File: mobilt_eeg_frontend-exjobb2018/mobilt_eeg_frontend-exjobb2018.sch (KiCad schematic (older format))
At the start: 86 parts, among them J1 Conn_02x04_Odd_Even, J2 Conn_02x08_Odd_Even, J3 Conn_02x08_Odd_Even, P1 Conn_02x20_Odd_Even, U1 ADS1299-4PAG, X1 X1G0044810050_SG7050CAN_2.048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

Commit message: Before annotation.
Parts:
- added J?: Conn_01x01, symbol Connector_Generic:Conn_01x01
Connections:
- wire segments 307 -> 308
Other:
- note added: "Test Point INTERNAL_VREF 4.5V"
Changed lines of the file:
@@
 Text Label 3950 5550 2    50   ~ 0
 IN8P
+$Comp
+L Connector_Generic:Conn_01x01 J?
+U 1 1 5BD5918B
+P 14000 6100
+F 0 "J?" H 14080 6142 50  0000 L CNN
+F 1 "Conn_01x01" H 14080 6051 50  0000 L CNN
+F 2 "" H 14000 6100 50  0001 C CNN
+F 3 "~" H 14000 6100 50  0001 C CNN
+	1    14000 6100
+	1    0    0    -1
+$EndComp
+Text Notes 14200 6100 0    50   ~ 0
+Test Point INTERNAL_VREF 4.5V
+Wire Wire Line
+	13800 6100 13500 6100
+Connection ~ 13500 6100
 $EndSCHEMATC

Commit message: beginning to understand the big picture... life, the universe, everything...
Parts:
- added C? (x9): 4.7nF, symbol Device:C_Small
- added J?: Conn_02x04_Odd_Even, symbol Connector_Generic:Conn_02x04_Odd_Even
- added J?: INT_CLK, symbol Connector_Generic:Conn_01x02
- added J?: Conn_01x10, symbol Connector_Generic:Conn_01x10
- added R? (x5): 10k, symbol Device:R
- added R? (x10): 4.99k 1%, symbol Device:R_Small
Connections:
- net labels added: CLKSEL
- wire segments 308 -> 360
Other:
- note added: "100nF not in datasheet."
- note added: ">=10k pulldown"
- note added: "Bias Signals"
- note added: "Electrodes [HIGH]/BIAS Header + filtering"
- note added: "Electrodes [LOW]/SRB Header + filtering"
- note added: "Feedback Elements\n(ch.9.3.2.4.1) \nTyp. values for example only"
- note added: "Pull down; DEFAULT EXT. CLK"
- note removed: "Bias Signals\nCHECK THIS SHIT"
- note removed: "Electrode Headers"
- moved on the sheet: C?, J?, R?, U?

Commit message: back it up my dude
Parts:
- removed J2, J3: Conn_02x08_Odd_Even, Pin_Headers:Pin_Header_Straight_2x08_Pitch2.54mm, symbol Connector_Generic:Conn_02x08_Odd_Even
- removed J?: Conn_02x20_Odd_Even, symbol Connector_Generic:Conn_02x20_Odd_Even
- removed J? (x2): Conn_01x10, symbol Connector_Generic:Conn_01x10
- removed R?: 4.99k 1%, symbol Device:R_Small
- added Cf: 1.5nF, symbol Device:C
- added J?: Conn_01x02, symbol Connector_Generic:Conn_01x02
- added J?: Data Header, symbol Connector_Generic:Conn_01x10
- added J? (x2): Conn_01x01, symbol Connector_Generic:Conn_01x01
- added J?: Conn_02x20_Odd_Even, symbol Connector_Generic:Conn_02x20_Odd_Even
- added Rf: 1M, symbol Device:R
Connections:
- net labels added: +3V3_Pi, BIASOUT_FILTERED, SRB1_FILT, SRB2_FILT
- wire segments 360 -> 387
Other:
- note added: "<-In case we need to bypass external reg."
- note added: "Bias Amp\nDC gain\n-(Rf*N)/330k)\n,where N channels."
- note added: "Bias/reference Signals"
- note added: "Cf sets bandwidth\nof Bias Amp."
- note added: "Data Header"
- note added: "Do Not Populate \nfor ADS1299-4!"
- note added: "Electrodes [HIGH]/BIASOUT Header + filtering"
- note added: "External BIASREF circuitry?"
- note added: "For 4ch., Rf=500k?"
- note added: "In case we need to bypass extern reg."
- note added: "Necessary??"
- note added: "PULLUP??"
- note added: "Post-Input filtering \n(ease of measurement)"
- note added: "Test Pad INTERNAL_VREF 4.5V"
- note added: "VCAP1 & 4 closest to ADS1299"
- note added: "VCAP1 Tantalum (not piezoelectric)"
- note added: "Yes, indeed..."
- note removed: "100nF not in datasheet."
- note removed: "ADC Bypassing/Filtering"
- note removed: "Bias Signals"
- note removed: "Electrodes [HIGH]/BIAS Header + filtering"
- note removed: "Tantalum?"
- note removed: "Test Point INTERNAL_VREF 4.5V"
- moved on the sheet: C?, D?, J?, R?, SW?, U?

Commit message: before new annotation
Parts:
- removed C?: 1.5nF, symbol Device:C
- removed J?: Conn_01x02, symbol Connector_Generic:Conn_01x02
- removed R?: 1M, symbol Device:R
- added C? (x5): 1uF, symbol Device:C
- added C? (x3): 100nF, symbol Device:C
- added D?: LED, symbol Device:LED
- added R?: 1k, symbol Device:R
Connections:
- net labels added: AVSS1
- net labels removed: GNDA, VSSA
- wire segments 387 -> 500
- no-connect marks 26 -> 24
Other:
- note added: "<-Regular"
- note added: "BIASIN left floating."
- note added: "From Pin descriptions\nch.6"
- note added: "RasPi Status LED 1"
- note added: "RasPi Status LED 2"
- note added: "Use 3mm THD\nuntil SMD package size\nresolved."
- note added: "pin 53"
- note added: "pin 54"
- note added: "pin 58"
- note added: "pin 59"
- note removed: "External BIASREF circuitry?"
- note removed: "Necessary??"
- note removed: "RasPi Status LED"
- moved on the sheet: C?, J?, R?, U?

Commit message: assigned PCB footprints
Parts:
- C10, C11, C12, C13, C14, C15, C16, C17, C18, C19, C2, C20, C21, C22, C23, C24, C25, C26, C27, C28, C29, C3, C30, C31, C32, C33, C34, C35, C36, C37, C38, C39, C4, C40, C41, C42, C43, C44, C48, C49, C5, C50, C51, C52, C53, C54, C55, C56, C57, C58, C59, C6, C60, C61, C7, C8, C9: renamed from C?; footprint (none) -> Capacitors_SMD:C_0805_HandSoldering
- C46, C47: renamed from C?; footprint (none) -> Capacitors_Tantalum_SMD:CP_Tantalum_Case-D_EIA-7343-31_Hand
- Cf1: renamed from Cf; footprint (none) -> Capacitors_SMD:C_0805_HandSoldering
- D1, D2: renamed from D?; footprint (none) -> LEDs:LED_D3.0mm
- J10, J6: renamed from J?; footprint (none) -> TestPoint:TestPoint_Pad_D2.0mm
- J11, J7: renamed from J?; footprint (none) -> Pin_Headers:Pin_Header_Straight_1x02_Pitch2.54mm
- J12, J4: renamed from J?; footprint (none) -> Pin_Headers:Pin_Header_Straight_1x01_Pitch2.54mm
- J2: renamed from J?; footprint (none) -> Pin_Headers:Pin_Header_Straight_2x20_Pitch2.54mm
- J3: renamed from J?; footprint (none) -> Pin_Headers:Pin_Header_Straight_2x04_Pitch2.54mm
- J5: renamed from J?; footprint (none) -> Pin_Headers:Pin_Header_Straight_1x10_Pitch2.54mm
- J8: renamed from J?; footprint (none) -> Pin_Headers:Pin_Header_Straight_1x08_Pitch2.54mm
- J9: renamed from J?; footprint (none) -> Pin_Headers:Pin_Header_Straight_1x04_Pitch2.54mm
- R10, R11, R12, R13, R14, R15, R16, R17, R18, R19, R20, R21, R22, R23, R24, R25, R26, R27, R28, R29, R3, R30, R31, R4, R5, R6, R7, R8, R9: renamed from R?; footprint (none) -> Resistors_SMD:R_0805_HandSoldering
- Rf1: renamed from Rf; footprint (none) -> Resistors_SMD:R_0805_HandSoldering
- SW1, SW2: renamed from SW?; footprint (none) -> Buttons_Switches_THT:SW_PUSH_6mm_h5mm
- U6: renamed from U?; footprint (none) -> Housings_SOIC:SOIC-8_3.9x4.9mm_Pitch1.27mm
- gave numbers to parts that had none: 5
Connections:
- wire segments 500 -> 499
- no-connect marks 24 -> 18
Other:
- note added: "DVDD: +3V3\nAVDD: +2V5\nAVSS: -2V5"
- note added: "Data Header \nBetween ADS1299 & RasPi"
- note added: "Probably go with 0805 [2012 metric]"
- note removed: "Data Header"
- moved on the sheet: C10, C11, C12, C2, C3, C32, C33, C34, C35, C36, C37, C38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

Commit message: 1/3 way there...
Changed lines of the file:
@@
 	1    0    0    -1
 $EndComp
-$Comp
-L power:GNDD #PWR0108
-U 1 1 5B46722C
-P 19150 3350
-F 0 "#PWR0108" H 19150 3100 50  0001 C CNN
-F 1 "GNDD" H 19154 3195 50  0000 C CNN
-F 2 "" H 19150 3350 50  0001 C CNN
-F 3 "" H 19150 3350 50  0001 C CNN
-	1    19150 3350
-	1    0    0    -1
-$EndComp
-$Comp
-L power:GNDD #PWR0109
-U 1 1 5B467375
-P 18450 3350
-F 0 "#PWR0109" H 18450 3100 50  0001 C CNN
-F 1 "GNDD" H 18454 3195 50  0000 C CNN
-F 2 "" H 18450 3350 50  0001 C CNN
-F 3 "" H 18450 3350 50  0001 C CNN
-	1    18450 3350
-	1    0    0    -1
-$EndComp
 NoConn ~ 10450 4400
 Text Notes 15000 900  0    50   ~ 0
@@
 	1    0    0    -1
 $EndComp
-Text Label 16000 6400 3    50   ~ 0
-+3V3
 $Comp
 L project_symbols:DGND #PWR0133
@@
 Text Notes 20050 6900 0    50   ~ 0
 Probably go with 0805 [2012 metric]
+$Comp
+L project_symbols:DVDD #PWR0105
+U 1 1 5FFDB454
+P 16000 6400
+F 0 "#PWR0105" H 16000 6250 50  0001 C CNN
+F 1 "DVDD" H 16018 6573 50  0000 C CNN
+F 2 "" H 16000 6400 50  0001 C CNN
+F 3 "" H 16000 6400 50  0001 C CNN
+	1    16000 6400
+	-1   0    0    1
+$EndComp
+$Comp
+L project_symbols:DGND #PWR?
+U 1 1 5FFE450C
+P 19150 3350
+F 0 "#PWR?" H 19150 3100 50  0001 C CNN
+F 1 "DGND" H 19154 3195 50  0000 C CNN
+F 2 "" H 19150 3350 50  0001 C CNN
+F 3 "" H 19150 3350 50  0001 C CNN
+	1    19150 3350
+	1    0    0    -1
+$EndComp
+$Comp
+L project_symbols:DGND #PWR?
+U 1 1 5FFE4612
+P 18450 3350
+F 0 "#PWR?" H 18450 3100 50  0001 C CNN
+F 1 "DGND" H 18454 3195 50  0000 C CNN
+F 2 "" H 18450 3350 50  0001 C CNN
+F 3 "" H 18450 3350 50  0001 C CNN
+	1    18450 3350
+	1    0    0    -1
+$EndComp
 $EndSCHEMATC

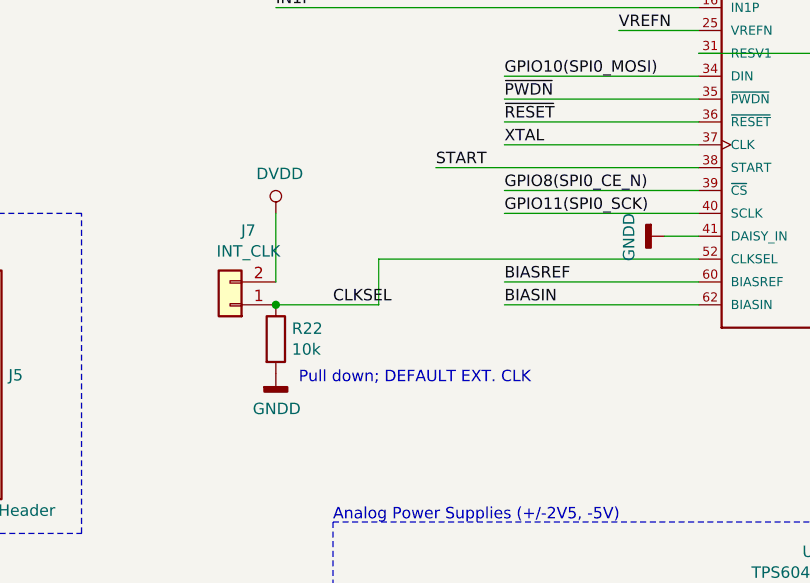
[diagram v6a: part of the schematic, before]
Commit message: took out CLKSEL jumper
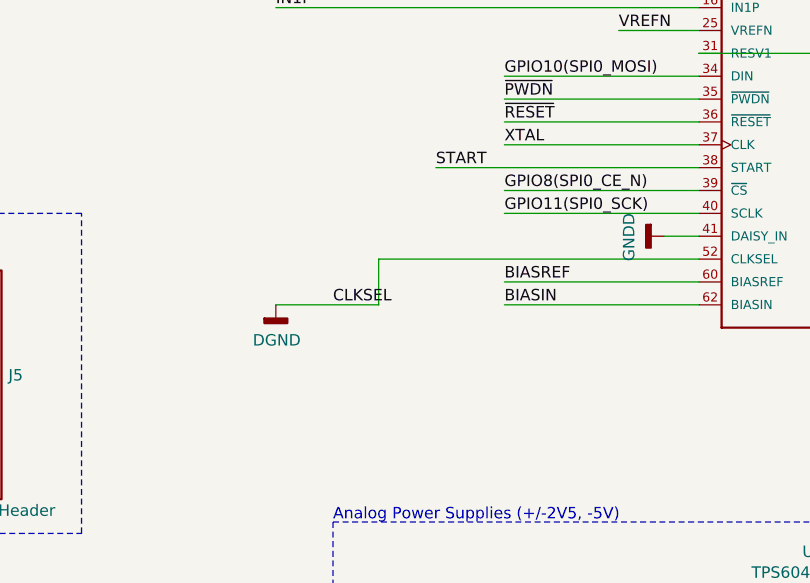
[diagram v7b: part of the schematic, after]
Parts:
- removed J7: INT_CLK, Pin_Headers:Pin_Header_Straight_1x02_Pitch2.54mm, symbol Connector_Generic:Conn_01x02
- removed R22: 10k, Resistors_SMD:R_0805_HandSoldering, symbol Device:R
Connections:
- wire segments 499 -> 498
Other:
- note removed: "Pull down; DEFAULT EXT. CLK"
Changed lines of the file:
@@
 CLKSEL
-$Comp
-L power:GNDD #PWR015
-U 1 1 5B6FFE3E
-P 6800 5500
-F 0 "#PWR015" H 6800 5250 50  0001 C CNN
-F 1 "GNDD" H 6804 5345 50  0000 C CNN
-F 2 "" H 6800 5500 50  0001 C CNN
-F 3 "" H 6800 5500 50  0001 C CNN
-	1    6800 5500
-	1    0    0    -1
-$EndComp
-$Comp
-L Device:R R22
-U 1 1 5B700D8A
-P 6800 5350
-F 0 "R22" H 6870 5396 50  0000 L CNN
-F 1 "10k" H 6870 5305 50  0000 L CNN
-F 2 "Resistors_SMD:R_0805_HandSoldering" V 6730 5350 50  0001 C CNN
-F 3 "~" H 6800 5350 50  0001 C CNN
-	1    6800 5350
-	1    0    0    -1
-$EndComp
-Text Notes 6900 5550 0    50   ~ 0
-Pull down; DEFAULT EXT. CLK
-$Comp
-L Connector_Generic:Conn_01x02 J7
-U 1 1 5B72A277
-P 6600 5200
-F 0 "J7" H 6520 4875 50  0000 C CNN
-F 1 "INT_CLK" H 6520 4966 50  0000 C CNN
-F 2 "Pin_Headers:Pin_Header_Straight_1x02_Pitch2.54mm" H 6600 5200 50  0001 C CNN
-F 3 "~" H 6600 5200 50  0001 C CNN
-	1    6600 5200
-	-1   0    0    1
-$EndComp
-Connection ~ 6800 5200
-$Comp
-L project_symbols:DVDD #PWR014
-U 1 1 5B72B59C
-P 6800 4800
-F 0 "#PWR014" H 6800 4650 50  0001 C CNN
-F 1 "DVDD" H 6817 4973 50  0000 C CNN
-F 2 "" H 6800 4800 50  0001 C CNN
-F 3 "" H 6800 4800 50  0001 C CNN
-	1    6800 4800
-	1    0    0    -1
-$EndComp
-Wire Wire Line
-	6800 4800 6800 5100
 $Comp
 L project_symbols:DGND #PWR027
@@
 $EndComp
 $Comp
-L project_symbols:DGND #PWR?
+L project_symbols:DGND #PWR0108
 U 1 1 5FFE450C
 P 19150 3350
-F 0 "#PWR?" H 19150 3100 50  0001 C CNN
+F 0 "#PWR0108" H 19150 3100 50  0001 C CNN
 F 1 "DGND" H 19154 3195 50  0000 C CNN
 F 2 "" H 19150 3350 50  0001 C CNN
@@
 $EndComp
 $Comp
-L project_symbols:DGND #PWR?
+L project_symbols:DGND #PWR0109
 U 1 1 5FFE4612
 P 18450 3350
-F 0 "#PWR?" H 18450 3100 50  0001 C CNN
+F 0 "#PWR0109" H 18450 3100 50  0001 C CNN
 F 1 "DGND" H 18454 3195 50  0000 C CNN
 F 2 "" H 18450 3350 50  0001 C CNN
@@
 	1    0    0    -1
 $EndComp
+$Comp
+L project_symbols:DGND #PWR?
+U 1 1 600A3D2E
+P 6800 5200
+F 0 "#PWR?" H 6800 4950 50  0001 C CNN
+F 1 "DGND" H 6804 5045 50  0000 C CNN
+F 2 "" H 6800 5200 50  0001 C CNN
+F 3 "" H 6800 5200 50  0001 C CNN
+	1    6800 5200
+	1    0    0    -1
+$EndComp

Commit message: Enough for today.
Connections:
- net labels removed: +3V3
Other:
- note added: "Star connect these ->"
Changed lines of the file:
@@
 Connection ~ 16750 1500
 $Comp
-L power:GNDD #PWR0104
-U 1 1 5B466A38
-P 10550 5300
-F 0 "#PWR0104" H 10550 5050 50  0001 C CNN
-F 1 "GNDD" H 10554 5145 50  0000 C CNN
-F 2 "" H 10550 5300 50  0001 C CNN
-F 3 "" H 10550 5300 50  0001 C CNN
-	1    10550 5300
-	1    0    0    -1
-$EndComp
-$Comp
 L power:GNDD #PWR0107
 U 1 1 5B466EBF
@@
 	13200 1300 12950 1300
 Text Label 12950 1200 2    50   ~ 0
-+3V3
++3V3_Pi
 Wire Wire Line
 	12950 1200 13200 1200
@@
 $EndComp
 $Comp
-L project_symbols:DGND #PWR?
+L project_symbols:DGND #PWR0111
 U 1 1 600A3D2E
 P 6800 5200
-F 0 "#PWR?" H 6800 4950 50  0001 C CNN
+F 0 "#PWR0111" H 6800 4950 50  0001 C CNN
 F 1 "DGND" H 6804 5045 50  0000 C CNN
 F 2 "" H 6800 5200 50  0001 C CNN
@@
 	1    0    0    -1
 $EndComp
+Text Notes 12050 5650 0    50   ~ 0
+Star connect these ->
+$Comp
+L project_symbols:DGND #PWR0104
+U 1 1 600ACC50
+P 10550 5300
+F 0 "#PWR0104" H 10550 5050 50  0001 C CNN
+F 1 "DGND" H 10554 5145 50  0000 C CNN
+F 2 "" H 10550 5300 50  0001 C CNN
+F 3 "" H 10550 5300 50  0001 C CNN
+	1    10550 5300
+	1    0    0    -1
+$EndComp
